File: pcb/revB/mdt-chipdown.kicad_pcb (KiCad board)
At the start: 4 copper layers, 94 x 79.6 mm, 134 parts, among them J1 BI, J2 BI, J3 SPDIF OUT, J4 Micro_SD_Card, J5 Micro_SD_Card, Q1 DMG2305UX, SW1 ON_OFF, SW2 PROGRAM, U1 TPD3S014, U10 TLV75733PDBV, U2 AMS1117-3.3, U3 ILI9341 3.2" capacitive touch, U4 PCM5102A, U5 APS6404L-3SQR, U6 APS6404L-3SQR, U7 MKL02Z32VFG4, U8 GD25Q64ESIGR, U9 MIMXRT1062DVJ6B, Y1 24MHz, Y2 32768

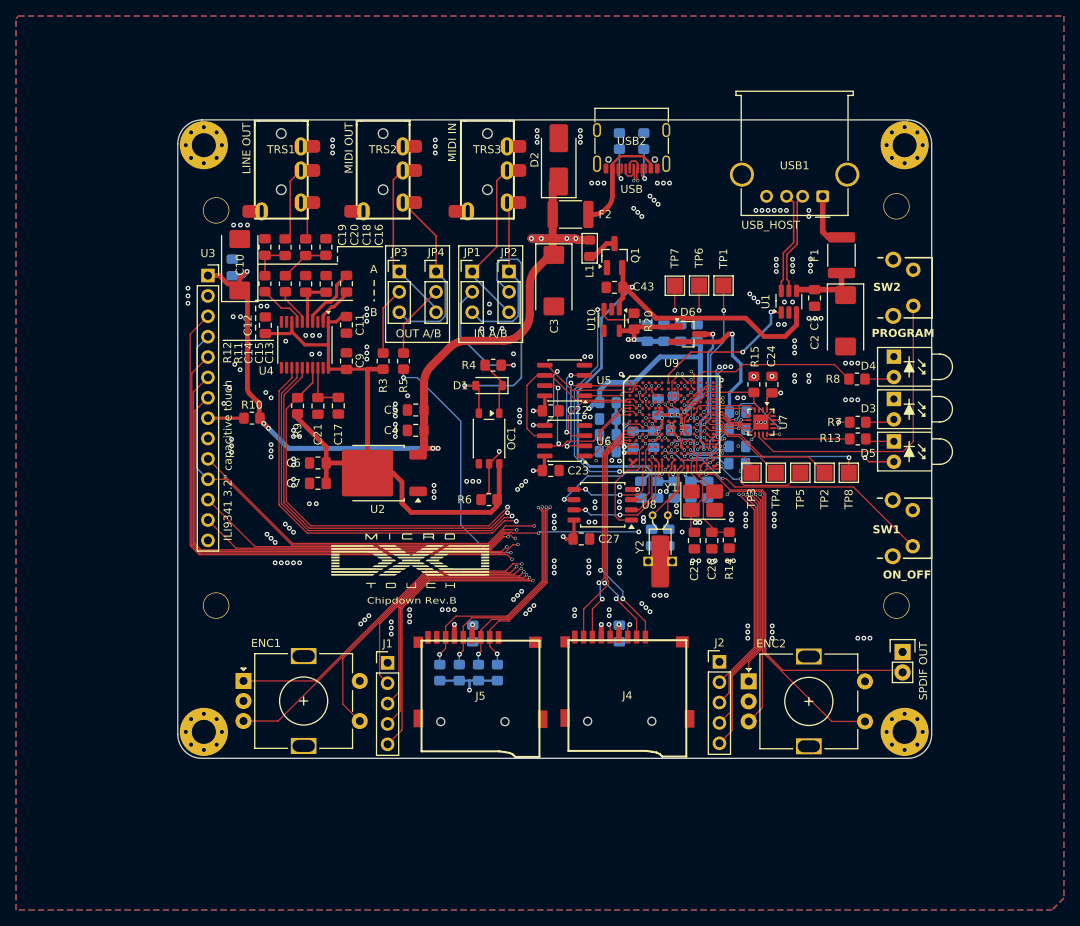
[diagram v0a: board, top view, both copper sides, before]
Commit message: Updated revB: changed vias from 0.4/0.3 to 0.45/0.2
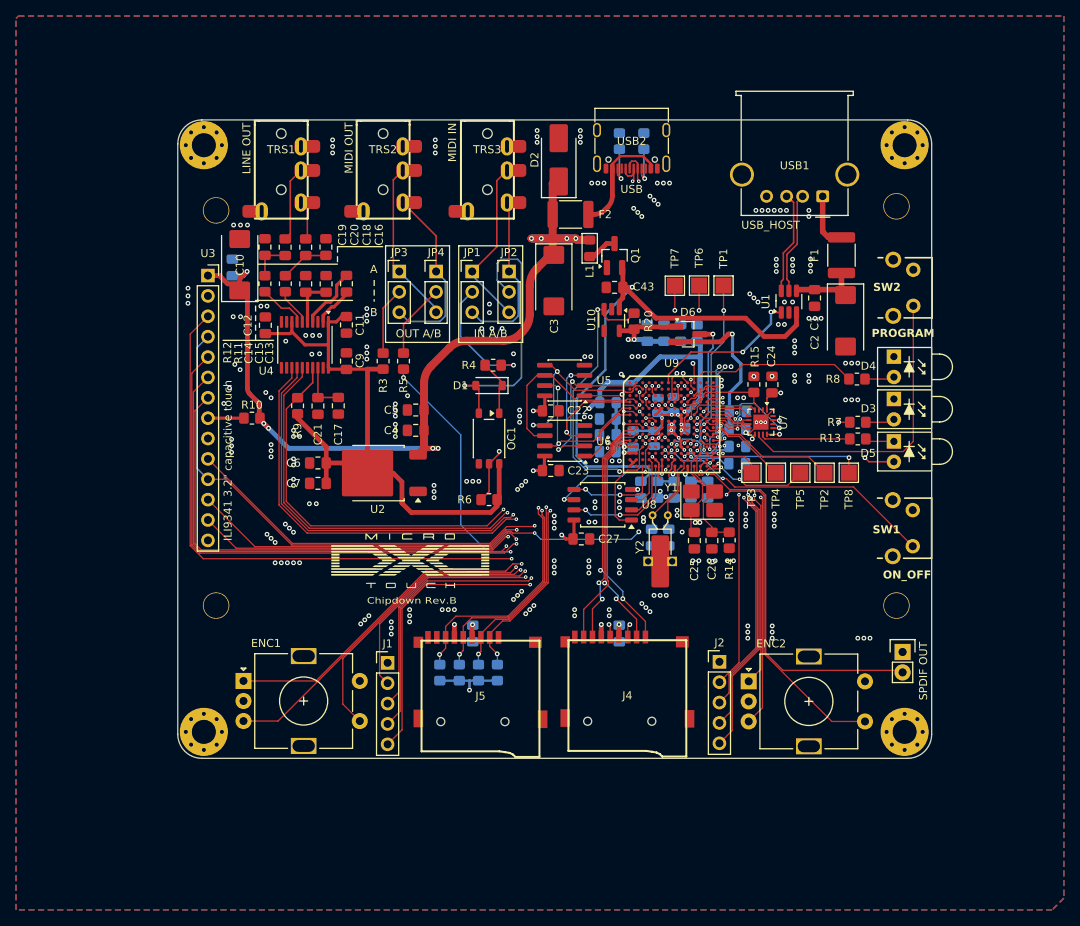
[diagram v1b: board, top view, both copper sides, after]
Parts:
- C37, C42, C47, C51: footprint Capacitor_SMD:C_0805_2012Metric_Pad1.18x1.45mm_HandSolder -> Capacitor_SMD:C_0805_2012Metric
- L3: footprint PCM_Inductor_SMD_AKL:L_0805_2012Metric_Pad1.15x1.40mm_HandSolder -> PCM_Inductor_SMD_AKL:L_0805_2012Metric_Pad1.15x1.40mm
- moved C37 0.18 mm to (107.9, 69.5)
- moved C47 0.18 mm to (110.5, 72.4)
- moved C51 0.11 mm to (107.5, 73.7)
- moved C34 0.08 mm to (117.9, 70.3)
- moved L3 0.05 mm to (104.8, 73.7)
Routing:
- net ENC_R_A: track 53.0 -> 102.2 mm
- net /MCU/MK9: track 17.4 -> 24.1 mm
- net USBH_DN: track 69.7 -> 74.3 mm
- net USB_DP: track 62.3 -> 66.7 mm
- net USB_DN: track 62.7 -> 67.1 mm
- net USBH_DP: track 69.3 -> 73.4 mm
- net BI_SEL: track 46.2 -> 43.9 mm
- net PSRAM_D1: track 18.8 -> 21.0 mm
- net (no net): track 2.10 -> 0.00 mm
- net GND: track 41.9 -> 40.1 mm
- net BI_A: track 49.4 -> 51.0 mm
- net ~{MUTE}: track 92.0 -> 90.6 mm
- net ENC_R_B: track 56.8 -> 55.6 mm
- net ~{MEM_CS}: track 27.5 -> 26.3 mm
- net TX: track 64.2 -> 63.1 mm
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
